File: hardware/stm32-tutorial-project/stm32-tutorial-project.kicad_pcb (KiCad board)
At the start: 2 copper layers, 72 parts, among them J1 USB_C_Receptacle_USB2.0_14P, J2 10pin IDC SWD, J3 Conn_01x04, J4 Conn_01x04, J5 Conn_01x13, J6 Conn_01x13, Q1 NPN, Q3 PNP, SW1 SW_Push, SW2 SW_Push_SPDT, U1 STM32G431CBTx, U2 AZ1117-3.3, X1 Crystal_GND24

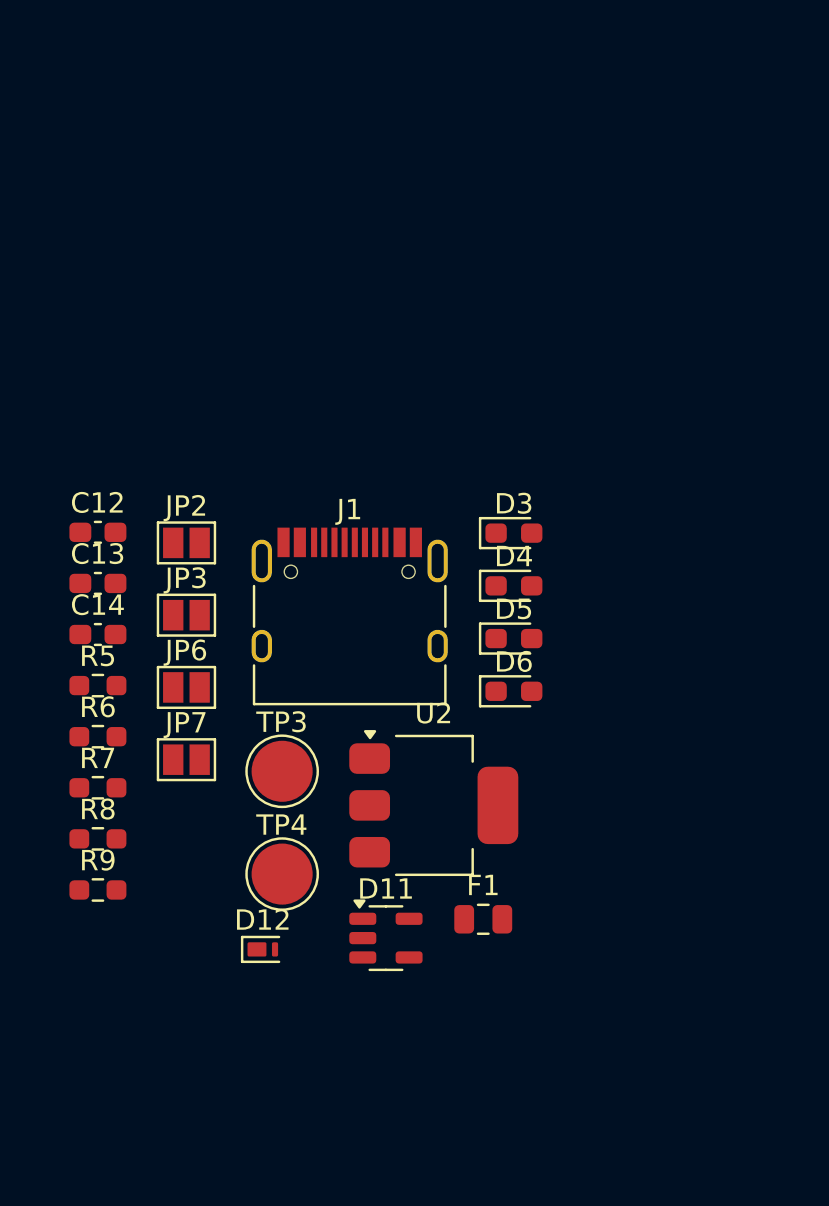
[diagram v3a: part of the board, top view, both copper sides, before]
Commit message: Begin iteration on USB connection/regulator path
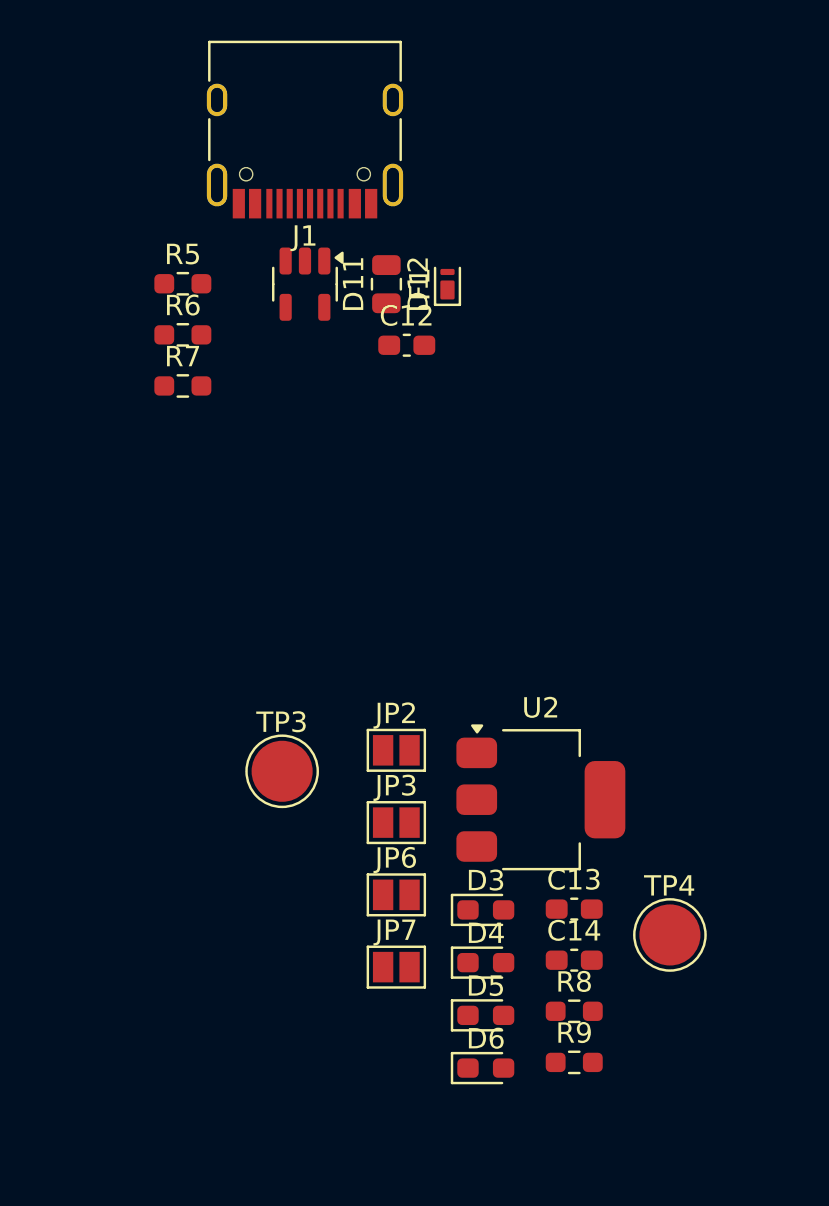
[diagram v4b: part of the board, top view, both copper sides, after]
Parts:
- moved D12 33.9 mm to (131.9, 27.0), turned to 90 degrees
- moved D11 32.4 mm to (124.9, 27.0), turned to -90 degrees
- moved F1 31.6 mm to (128.9, 27.0), turned to -90 degrees
- moved C13 28.3 mm to (138.1, 57.7)
- moved C14 28.3 mm to (138.1, 60.2)
- moved R8 24.9 mm to (138.1, 62.7)
- moved R9 24.9 mm to (138.1, 65.2)
- moved J1 24.8 mm to (124.9, 19.0), turned to 180 degrees
- moved R7 20.2 mm to (118.9, 32.0)
- moved R5 20.2 mm to (118.9, 27.0)
- moved R6 20.2 mm to (118.9, 29.5)
- moved TP4 19.3 mm to (142.8, 59.0)
- moved D3 18.6 mm to (133.7, 57.7)
- moved D5 18.6 mm to (133.7, 62.9)
- moved D6 18.6 mm to (133.7, 65.5)
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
